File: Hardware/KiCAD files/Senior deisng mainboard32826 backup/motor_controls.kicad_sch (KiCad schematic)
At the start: 276 parts, among them Q1 DMHT6016LFJ, Q10 DMHT6016LFJ, Q11 DMHT6016LFJ, Q12 DMHT6016LFJ, Q2 DMHT6016LFJ, Q3 DMHT6016LFJ, Q4 DMHT6016LFJ, Q5 DMHT6016LFJ, Q6 DMHT6016LFJ, Q7 DMHT6016LFJ, Q8 DMHT6016LFJ, Q9 DMHT6016LFJ, U1 TMC2160, U2 TMC2160, U3 TMC2160, U5 TMC2160, U6 TMC2160, U7 TMC2160

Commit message: added more schematics for initial design
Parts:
- removed C10, C116, C117, C57, C58, C9: 470n 16V, Capacitor_SMD:C_0603_1608Metric_Wbry, symbol Device:C_Small
- removed C100, C101, C209, C210, C211, C212, C213, C214, C215, C216, C32, C33, C34, C35, C36, C37, C38, C39, C94, C95, C96, C97, C98, C99: 220n 100V, Capacitor_SMD:C_1206_3216Metric, symbol Device:C_Small
- removed C102, C103, C104, C105, C106, C107, C108, C109, C217, C218, C219, C220, C221, C222, C223, C224, C40, C41, C42, C44, C45, C46, C47, C48: 1n 100V, Capacitor_SMD:C_0603_1608Metric_Wbry, symbol Device:C_Small
- removed C11, C118, C119, C12, C122, C123, C16, C17, C59, C60, C69, C75: 2n2 50V, Capacitor_SMD:C_0402_1005Metric_Wbry, symbol Device:C_Small
- removed C110, C111, C112, C113, C2, C4, C49, C5, C50, C52, C53, C6: 2u2 16V, Capacitor_SMD:C_0603_1608Metric_Wbry, symbol Device:C_Small
- removed C114, C115, C54, C56, C7, C8: 0u1 10V, Capacitor_SMD:C_0402_1005Metric_Wbry, symbol Device:C_Small
- removed C120, C121, C124, C125, C13, C130, C131, C132, C133, C14, C18, C19, C24, C25, C26, C27, C67, C68, C76, C77, C82, C83, C84, C85: 220n 16V, Capacitor_SMD:C_0603_1608Metric_Wbry, symbol Device:C_Small
- removed C126, C127, C134, C135, C20, C21, C28, C29, C78, C79, C87, C91: 0u1 100V, Capacitor_SMD:C_0603_1608Metric_Wbry, symbol Device:C_Small
- removed C128, C129, C22, C23, C80, C81: 22n X7R 10% 100V, Capacitor_SMD:C_0603_1608Metric_Wbry, symbol Device:C_Small
- removed C207, C208, C30, C31, C92, C93: 220u 63V, Capacitor_THT:CP_Radial_D10.0mm_P5.00mm, symbol Device:CP1_Small
- removed D38, D39, D40, D41, D42, D43, D44, D45, D46, D47, D48, D49, D50, D51, D52, D53, D54, D55, D56, D57, D58, D59, D60, D61: BAT40V, Package_TO_SOT_SMD:SOT-563, symbol Duet3:BAT40V
- removed NT10, NT11, NT12, NT13, NT14, NT3, NT4, NT5, NT6, NT7, NT8, NT9: NT_SBG, NetTie:NetTie-2_SMD_Pad0.25mm, symbol Device:NetTie_2
- removed Q1, Q10, Q11, Q12, Q2, Q3, Q4, Q5, Q6, Q7, Q8, Q9: DMHT6016LFJ, complib:DMHT6016LFJ-13, symbol Duet3:Q_QUAD_NMOS_DMHT6016LFJ-1
- removed R10, R11, R12, R13, R14, R15, R19, R208, R209, R210, R211, R212, R213, R214, R215, R79, R80, R81, R82, R9, R95, R96, R97, R98: 47R 1%, Resistor_SMD:R_0402_1005Metric_Wbry, symbol Device:R_Small
- removed R100, R101, R189, R190, R191, R192, R193, R194, R195, R196, R197, R198, R199, R200, R201, R216, R217, R218, R219, R220, R221, R222, R223, R224, R225, R226, R227, R228, R229, R230, R231, R25, R26, R36, R37, R38, R55, R60, R61, R62, R63, R64, R65, R66, R67, R68, R69, R99: 150R, Resistor_SMD:R_0402_1005Metric_Wbry, symbol Device:R_Small
- removed R202, R203, R204, R205, R232, R233, R234, R235, R70, R71, R75, R76: 0R05 1% 1W, Resistor_SMD:R_1206_3216Metric_Pad1.24x1.80mm_HandSolder, symbol Device:R_Small
- removed R206, R207, R5, R6, R77, R78: 2R2 1%, Resistor_SMD:R_0402_1005Metric_Wbry, symbol Device:R_Small
- removed U1, U2, U3, U5, U6, U7: TMC2160, complib:TMC5160-TA, symbol Duet3:TMC5160-TA
- added C2: 10nF, PCM_SparkFun-Capacitor:C_0603_1608Metric, symbol PCM_SparkFun-Capacitor:10nF_0603_50V_10%
- added C4: 0.1uF, PCM_SparkFun-Capacitor:C_0603_1608Metric, symbol PCM_SparkFun-Capacitor:0.1uF_0603_25V_20%
- added J1, J2: Conn_01x08, PCM_SparkFun-Connector:1x08_P2.54mm, symbol PCM_SparkFun-Connector:Conn_01x08_P2.54mm
- added U1: DRV8825PWPR, PWP28_5P18X3P1, symbol DRV8825PRPR driver chip:DRV8825PWPR
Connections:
- new net: C2.1, U1.1 (CP1)
- new net: C2.2, U1.2 (CP2)
- new net: C4.2, U1.3 (VCP)
- new net A1: J2.5 (Pin_5), U1.5 (AOUT1)
- new net A2: J2.6 (Pin_6), U1.7 (AOUT2)
- new net B1: J2.4 (Pin_4), U1.10 (BOUT1)
- new net B2: J2.3 (Pin_3), U1.8 (BOUT2)
- new net VMM: C4.1, U1.11 (VMB), U1.4 (VMA)
- no-connect marks 12 -> 0
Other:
- note removed: "Driver 0"
- note removed: "Driver 1"
- note removed: "Driver 2"
- note removed: "Driver 3"
- note removed: "Driver 4"
- note removed: "Driver 5"

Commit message: DRV8825 initial design
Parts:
- added C5: 470nF, PCM_SparkFun-Capacitor:C_0402_1005Metric, symbol PCM_SparkFun-Capacitor:470nF_0402_25V_10%
- added R5: 10k Linear, PCM_SparkFun-Resistor:Bourns-PDB18, symbol PCM_SparkFun-Resistor:Trimpot_10k_RA_PTH
- added R6: 1.5k, PCM_SparkFun-Resistor:R_0603_1608Metric, symbol PCM_SparkFun-Resistor:1.5k_0603
- added R9: 10k, PCM_SparkFun-Resistor:R_0603_1608Metric, symbol PCM_SparkFun-Resistor:10k_0603
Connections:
- net +3V3: now also U1.15 (V3P3OUT), C5.1, R5.3
- net VMM: now also J2.1 (Pin_1)
- net GND: now reaches J2.2 (Pin_2)
- net GND: now also J2.8 (Pin_8), U1.14 (GND), U1.28 (GND), U1.6 (ISENA), U1.9 (ISENB), C5.2, R5.1
- net at J2.7 (Pin_7): now also R6.2, R9.1
- net at J1.1 (Pin_1): now also U1.20 (DIR)
- net at J1.2 (Pin_2): now also U1.22 (STEP)
- net at J1.3 (Pin_3): now also U1.17 (NSLEEP)
- net at J1.4 (Pin_4): now also U1.16 (NRESET)
- net at J1.5 (Pin_5): now also U1.26 (MODE2)
- net at J1.6 (Pin_6): now also U1.25 (MODE1)
- net at J1.7 (Pin_7): now also U1.24 (MODE0)
- net at J1.8 (Pin_8): now also U1.21 (NENBL)
- net at U1.12 (AVREF): now also U1.13 (BVREF), R5.2
- net at U1.18 (NFAULT): now also R6.1
- new net SLP: R9.2
- no-connect marks 0 -> 4
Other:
- note added: "DRV8825 1.0 D0"
- note added: "NoteMeausure impedance of the lines in layout ISA and ISB are .10 ohm"

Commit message: Schematic adjustments made prior to initial submission to Chan thursday
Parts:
- added C6: 4.7uF, PCM_SparkFun-Capacitor:C_0603_1608Metric, symbol PCM_SparkFun-Capacitor:4.7uF_0603_35V_20%
- added C7, C8: 0.1uF, PCM_SparkFun-Capacitor:C_0603_1608Metric, symbol PCM_SparkFun-Capacitor:0.1uF_0603_25V_20%
- added J4: JST_SMD_1.0mm_Vertical, PCM_SparkFun-Connector:JST_1x04_P1.0mm_Vertical_SMD, symbol PCM_SparkFun-Connector:Conn_01x04_JST_P1.0mm_Vertical_SMD
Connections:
- net GND: now also C6.2, C7.2, C8.2
- net VMM: now also C6.1, C7.1, C8.1
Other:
- note added: "A1-A2, B1-B2 phases for stepper motors"
- note added: "This is designed as a standalone, J1 and J2 removed for mainboard."
- moved on the sheet: R6

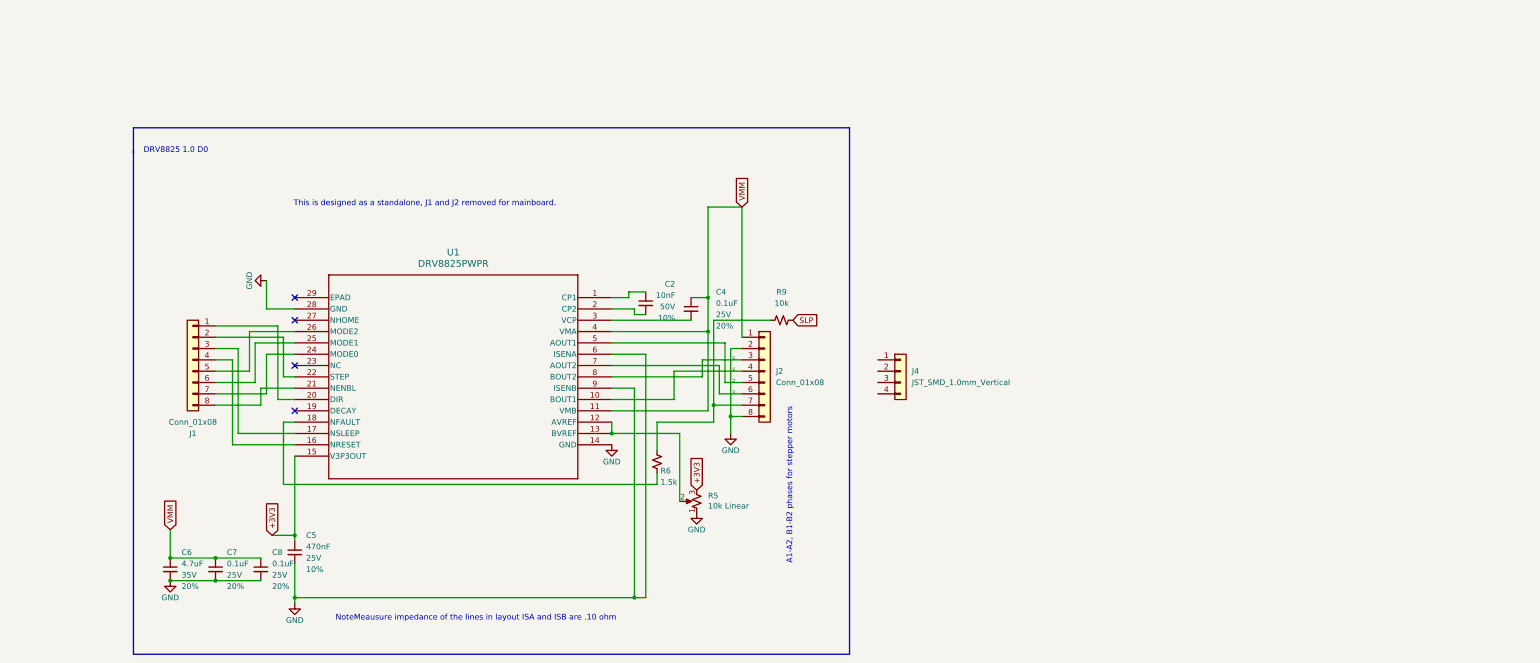
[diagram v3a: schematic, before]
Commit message: MCU power, new MCU placed, LCD communication, AC coupling of voltage reg on MCU
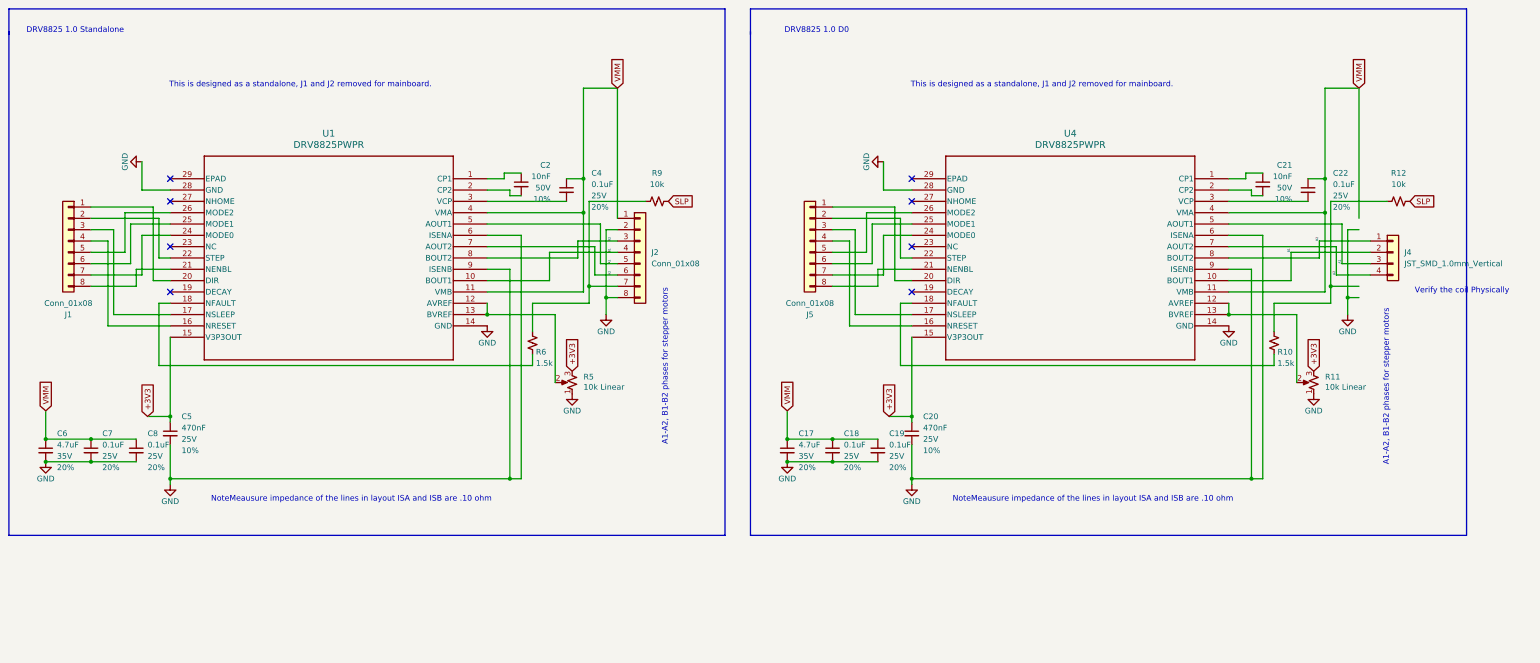
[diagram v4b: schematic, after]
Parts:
- added C17: 4.7uF, PCM_SparkFun-Capacitor:C_0603_1608Metric, symbol PCM_SparkFun-Capacitor:4.7uF_0603_35V_20%
- added C18, C19, C22: 0.1uF, PCM_SparkFun-Capacitor:C_0603_1608Metric, symbol PCM_SparkFun-Capacitor:0.1uF_0603_25V_20%
- added C20: 470nF, PCM_SparkFun-Capacitor:C_0402_1005Metric, symbol PCM_SparkFun-Capacitor:470nF_0402_25V_10%
- added C21: 10nF, PCM_SparkFun-Capacitor:C_0603_1608Metric, symbol PCM_SparkFun-Capacitor:10nF_0603_50V_10%
- added J5: Conn_01x08, PCM_SparkFun-Connector:1x08_P2.54mm, symbol PCM_SparkFun-Connector:Conn_01x08_P2.54mm
- added R10: 1.5k, PCM_SparkFun-Resistor:R_0603_1608Metric, symbol PCM_SparkFun-Resistor:1.5k_0603
- added R11: 10k Linear, PCM_SparkFun-Resistor:Bourns-PDB18, symbol PCM_SparkFun-Resistor:Trimpot_10k_RA_PTH
- added R12: 10k, PCM_SparkFun-Resistor:R_0603_1608Metric, symbol PCM_SparkFun-Resistor:10k_0603
- added U4: DRV8825PWPR, PWP28_5P18X3P1, symbol DRV8825PRPR driver chip:DRV8825PWPR
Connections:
- net +3V3: now also C20.1, R11.3, U4.15 (V3P3OUT)
- net A1: now also J4.3 (Pin_3), U4.5 (AOUT1)
- net A2: now also J4.4 (Pin_4), U4.7 (AOUT2)
- net B1: now also J4.2 (Pin_2), U4.10 (BOUT1)
- net B2: now also J4.1 (Pin_1), U4.8 (BOUT2)
- net GND: now also C17.2, C18.2, C19.2, C20.2, R11.1, U4.14 (GND), U4.28 (GND), U4.6 (ISENA), U4.9 (ISENB)
- net SLP: now also R12.2
- net VMM: now also C17.1, C18.1, C19.1, C22.1, U4.11 (VMB), U4.4 (VMA)
- new net: C21.1, U4.1 (CP1)
- new net: C21.2, U4.2 (CP2)
- new net: R10.1, U4.18 (NFAULT)
- new net: R10.2, R12.1
- new net: R11.2, U4.12 (AVREF), U4.13 (BVREF)
- new net: J5.4 (Pin_4), U4.16 (NRESET)
- new net: J5.3 (Pin_3), U4.17 (NSLEEP)
- new net: J5.1 (Pin_1), U4.20 (DIR)
- new net: J5.8 (Pin_8), U4.21 (NENBL)
- new net: J5.2 (Pin_2), U4.22 (STEP)
- new net: J5.7 (Pin_7), U4.24 (MODE0)
- new net: J5.6 (Pin_6), U4.25 (MODE1)
- new net: J5.5 (Pin_5), U4.26 (MODE2)
- new net: C22.2, U4.3 (VCP)
- no-connect marks 4 -> 8
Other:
- note added: "DRV8825 1.0 Standalone"
- note added: "Verify the coil Physically"
- moved on the sheet: C2, C4, C5, C6, C7, C8, J1, J2, J4, R5, R6, R9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

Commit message: IO pull resistors, Motor driver V1, LCD communication
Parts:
- removed C18, C19: 0.1uF, PCM_SparkFun-Capacitor:C_0603_1608Metric, symbol PCM_SparkFun-Capacitor:0.1uF_0603_25V_20%
- removed J5: Conn_01x08, PCM_SparkFun-Connector:1x08_P2.54mm, symbol PCM_SparkFun-Connector:Conn_01x08_P2.54mm
- added C10, C11, C19, C27, C31, C34, C35, C39, C42, C43, C47, C9: 0.1uF, PCM_SparkFun-Capacitor:C_0603_1608Metric, symbol PCM_SparkFun-Capacitor:0.1uF_0603_100V_10%
- added C12, C32, C40, C48: 100uF_50V, Capacitor_THT:CP_Radial_D8.0mm_P3.50mm, symbol PCM_SL_Capacitors:100uF_50V
- added C18, C33, C41: 4.7uF, PCM_SparkFun-Capacitor:C_0603_1608Metric, symbol PCM_SparkFun-Capacitor:4.7uF_0603_35V_20%
- added C28, C36, C44: 470nF, PCM_SparkFun-Capacitor:C_0402_1005Metric, symbol PCM_SparkFun-Capacitor:470nF_0402_25V_10%
- added C29, C37, C45: 10nF, PCM_SparkFun-Capacitor:C_0603_1608Metric, symbol PCM_SparkFun-Capacitor:10nF_0603_50V_10%
- added C30, C38, C46: 0.1uF, PCM_SparkFun-Capacitor:C_0603_1608Metric, symbol PCM_SparkFun-Capacitor:0.1uF_0603_25V_20%
- added J11, J12: Conn_01x08, PCM_SparkFun-Connector:1x08_P2.54mm, symbol PCM_SparkFun-Connector:Conn_01x08_P2.54mm
- added J16, J17, J18: JST_SMD_1.0mm_Vertical, PCM_SparkFun-Connector:JST_1x04_P1.0mm_Vertical_SMD, symbol PCM_SparkFun-Connector:Conn_01x04_JST_P1.0mm_Vertical_SMD
- added R16, R22, R27, R32: 1_Mohm, symbol PCM_Resistor_AKL:R_Generic
- added R19, R25, R30, R4: .2 ohm, symbol PCM_Resistor_AKL:R_Generic
- added R20, R26, R31: 1.5k, PCM_SparkFun-Resistor:R_0603_1608Metric, symbol PCM_SparkFun-Resistor:1.5k_0603
- added R23, R28, R33: 10k Linear, PCM_SparkFun-Resistor:Bourns-PDB18, symbol PCM_SparkFun-Resistor:Trimpot_10k_RA_PTH
- added R24, R29, R34: 10k, PCM_SparkFun-Resistor:R_0603_1608Metric, symbol PCM_SparkFun-Resistor:10k_0603
- added U10, U8, U9: DRV8825PWPR, PWP28_5P18X3P1, symbol DRV8825PRPR driver chip:DRV8825PWPR
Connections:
- net +3V3: now also C28.1, C36.1, C44.1, R23.3, R28.3, R33.3, U10.15 (V3P3OUT), U8.15 (V3P3OUT), U9.15 (V3P3OUT)
- net A1: now also J16.3 (Pin_3), J17.3 (Pin_3), J18.3 (Pin_3), U10.5 (AOUT1), U8.5 (AOUT1), U9.5 (AOUT1)
- net A2: now also J16.4 (Pin_4), J17.4 (Pin_4), J18.4 (Pin_4), U10.7 (AOUT2), U8.7 (AOUT2), U9.7 (AOUT2)
- net B1: now also J16.2 (Pin_2), J17.2 (Pin_2), J18.2 (Pin_2), U10.10 (BOUT1), U8.10 (BOUT1), U9.10 (BOUT1)
- net B2: now also J16.1 (Pin_1), J17.1 (Pin_1), J18.1 (Pin_1), U10.8 (BOUT2), U8.8 (BOUT2), U9.8 (BOUT2)
- net GND: now also C10.2, C11.2, C12.2, C18.2, C19.2, C27.2, C28.2, C31.2, C32.2, C33.2, C34.2, C35.2, C36.2, C39.2, C40.2, C41.2, C42.2, C43.2, C44.2, C47.2, C48.2, C9.2, J12.2 (Pin_2), J12.8 (Pin_8), R19.1, R23.1, R25.1, R28.1, R30.1, R33.1, R4.1, U10.14 (GND), U10.28 (GND), U8.14 (GND), U8.28 (GND), U9.14 (GND), U9.28 (GND); no longer U4.6 (ISENA), U4.9 (ISENB)
- net SLP: now also U4.17 (NSLEEP), J11.3 (Pin_3), R24.2, R29.2, R34.2, U10.17 (NSLEEP), U8.17 (NSLEEP), U9.17 (NSLEEP)
- net N_FAULT: now reaches R10.2, R12.1
- net N_FAULT: now also R20.2, R24.1, R26.2, R29.1, R31.2, R34.1
- net NRESET: now reaches U4.16 (NRESET)
- net NRESET: now also J11.4 (Pin_4), U10.16 (NRESET), U8.16 (NRESET), U9.16 (NRESET)
- net DIR: now reaches U4.20 (DIR)
- net DIR: now also J11.1 (Pin_1), U10.20 (DIR), U8.20 (DIR), U9.20 (DIR)
- net N_ENBL: now reaches U4.21 (NENBL)
- net N_ENBL: now also J11.8 (Pin_8), U10.21 (NENBL), U8.21 (NENBL), U9.21 (NENBL)
- net DRIVER_0_STEP: now reaches U4.22 (STEP)
- net MODE_0_GPIO: now reaches U4.24 (MODE0)
- net MODE_0_GPIO: now also J11.7 (Pin_7), U10.24 (MODE0), U8.24 (MODE0), U9.24 (MODE0)
- net MODE_1_GPIO: now reaches U4.25 (MODE1)
- net MODE_1_GPIO: now also J11.6 (Pin_6), U10.25 (MODE1), U8.25 (MODE1), U9.25 (MODE1)
- net MODE_2_GPIO: now reaches U4.26 (MODE2)
- net MODE_2_GPIO: now also J11.5 (Pin_5), U10.26 (MODE2), U8.26 (MODE2), U9.26 (MODE2)
- net at C22.2, U4.3 (VCP): now also R16.2
- net VMM renamed +24V
- net +24V: now also C10.1, C11.1, C12.1, C18.1, C19.1, C27.1, C30.1, C31.1, C32.1, C33.1, C34.1, C35.1, C38.1, C39.1, C40.1, C41.1, C42.1, C43.1, C46.1, C47.1, C48.1, C9.1, R16.1, R22.1, R27.1, R32.1, U10.11 (VMB), U10.4 (VMA), U8.11 (VMB), U8.4 (VMA), U9.11 (VMB), U9.4 (VMA)
- new net: C37.1, U9.1 (CP1)
- new net: C37.2, U9.2 (CP2)
- new net: R28.2, U9.12 (AVREF), U9.13 (BVREF)
- new net: R26.1, U9.18 (NFAULT)
- new net: C38.2, R27.2, U9.3 (VCP)
- new net: R25.2, U9.6 (ISENA), U9.9 (ISENB)
- new net: C30.2, R22.2, U8.3 (VCP)
- new net: R31.1, U10.18 (NFAULT)
- new net: R30.2, U10.6 (ISENA), U10.9 (ISENB)
- new net: R20.1, U8.18 (NFAULT)
- new net: C45.1, U10.1 (CP1)
- new net: C45.2, U10.2 (CP2)
- new net: R4.2, U4.6 (ISENA), U4.9 (ISENB)
- new net: C46.2, R32.2, U10.3 (VCP)
- new net: R33.2, U10.12 (AVREF), U10.13 (BVREF)
- new net: R19.2, U8.6 (ISENA), U8.9 (ISENB)
- new net: C29.1, U8.1 (CP1)
- new net: C29.2, U8.2 (CP2)
- new net: R23.2, U8.12 (AVREF), U8.13 (BVREF)
- new net DRIVER_1_STEP: U8.22 (STEP)
- new net DRIVER_2_STEP: U9.22 (STEP)
- new net DRIVER_3_STEP: U10.22 (STEP)
- new net STEP: J11.2 (Pin_2)
- no-connect marks 8 -> 20
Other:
- note added: "ALL NOTES FOR MOTOR DRIVER SCHEM"
- note added: "DRV8825 1.0 D02"
- note added: "DRV8825 1.0 D1"
- note added: "DRV8825 1.0 D3"
- note added: "For standalone testing"
- note added: "Max 8 ma"
- note added: "NoteMeausure impedance of the lines in layout ISA and ISB are .20 ohm, do with wire parasitics"
- note added: "Replace all generics for specific componenets"
- note added: "SLP @ fault"
- note added: "This is designed to be integrated only leaving a connector output to the stepper"
- moved on the sheet: C21, C22

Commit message: 1.1, devices have been cleaned up
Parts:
- removed J18: JST_SMD_1.0mm_Vertical, PCM_SparkFun-Connector:JST_1x04_P1.0mm_Vertical_SMD, symbol PCM_SparkFun-Connector:Conn_01x04_JST_P1.0mm_Vertical_SMD
- added C52: 4.7uF, PCM_SparkFun-Capacitor:C_0603_1608Metric, symbol PCM_SparkFun-Capacitor:4.7uF_0603_35V_20%
- added C53, C54, C58: 0.1uF, PCM_SparkFun-Capacitor:C_0603_1608Metric, symbol PCM_SparkFun-Capacitor:0.1uF_0603_100V_10%
- added C55: 470nF, PCM_SparkFun-Capacitor:C_0402_1005Metric, symbol PCM_SparkFun-Capacitor:470nF_0402_25V_10%
- added C56: 10nF, PCM_SparkFun-Capacitor:C_0603_1608Metric, symbol PCM_SparkFun-Capacitor:10nF_0603_50V_10%
- added C57: 0.1uF, PCM_SparkFun-Capacitor:C_0603_1608Metric, symbol PCM_SparkFun-Capacitor:0.1uF_0603_25V_20%
- added C59: 100uF_50V, Capacitor_THT:CP_Radial_D8.0mm_P3.50mm, symbol PCM_SL_Capacitors:100uF_50V
- added J29: JST_SMD_1.0mm_Vertical, PCM_SparkFun-Connector:JST_1x04_P1.0mm_Vertical_SMD, symbol PCM_SparkFun-Connector:Conn_01x04_JST_P1.0mm_Vertical_SMD
- added J5, J9: PINHD_1x8_Male, Connector_PinHeader_2.54mm:PinHeader_1x08_P2.54mm_Vertical, symbol PCM_SL_Pin_Headers:PINHD_1x8_Male
- added R39: .2 ohm, symbol PCM_Resistor_AKL:R_Generic
- added R40: 1.5k, PCM_SparkFun-Resistor:R_0603_1608Metric, symbol PCM_SparkFun-Resistor:1.5k_0603
- added R41: 1_Mohm, symbol PCM_Resistor_AKL:R_Generic
- added R42: 10k Linear, PCM_SparkFun-Resistor:Bourns-PDB18, symbol PCM_SparkFun-Resistor:Trimpot_10k_RA_PTH
- added R43: 10k, PCM_SparkFun-Resistor:R_0603_1608Metric, symbol PCM_SparkFun-Resistor:10k_0603
- added U5: DRV8825PWPR, PWP28_5P18X3P1, symbol DRV8825PRPR driver chip:DRV8825PWPR
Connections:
- net DRIVER_3_STEP is gone; now on net DRIVER_2_STEP: U10.22 (STEP)
- net +24V: now also C52.1, C53.1, C54.1, C57.1, C58.1, C59.1, J9.7, R41.1, U5.11 (VMB), U5.4 (VMA)
- net +3V3: now also C55.1, R42.3, U5.15 (V3P3OUT)
- net A1: now also J29.3 (Pin_3), J9.3, U5.5 (AOUT1)
- net A2: now also J29.4 (Pin_4), J9.4, U5.7 (AOUT2)
- net B1: now also J29.2 (Pin_2), J9.2, U5.10 (BOUT1)
- net B2: now also J29.1 (Pin_1), J9.1, U5.8 (BOUT2)
- net GND: now also C52.2, C53.2, C54.2, C55.2, C58.2, C59.2, J9.5, J9.8, R39.1, R42.1, U5.14 (GND), U5.28 (GND)
- net NRESET: now also J5.4, U5.16 (NRESET)
- net SLP: now also R43.2
- new net: J9.6, R40.2, R43.1
- new net: C56.1, U5.1 (CP1)
- new net: R42.2, U5.12 (AVREF), U5.13 (BVREF)
- new net: J5.3, U5.17 (NSLEEP)
- new net: R40.1, U5.18 (NFAULT)
- new net: C56.2, U5.2 (CP2)
- new net: J5.1, U5.20 (DIR)
- new net: J5.8, U5.21 (NENBL)
- new net: J5.2, U5.22 (STEP)
- new net: J5.7, U5.24 (MODE0)
- new net: J5.6, U5.25 (MODE1)
- new net: J5.5, U5.26 (MODE2)
- new net: C57.2, R41.2, U5.3 (VCP)
- new net: R39.2, U5.6 (ISENA), U5.9 (ISENB)
- no-connect marks 20 -> 24
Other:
- note added: "DRV8825 1.0 D03 Extruder"
- note added: "NEED TO RE-IMPLEMENT EXRUDER DRIVER, individual control necessary"
- note added: "Stand-alone DRV8825 1.0 D0"
- note added: "previous design for reference"
- note removed: "DRV8825 1.0 D3"
- moved on the sheet: C2, C4, C5, C6, C7, C8, J1, J2, R5, R6, R9, U1
